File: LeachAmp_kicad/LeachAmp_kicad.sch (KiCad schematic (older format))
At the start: 119 parts, among them J1 Conn_01x12_Female, J2 Conn_01x04_Female, J3 Conn_01x03_Female, J4 Conn_01x03_Female, Q1 BC546, Q10 MPSA06, Q11 MPSA56, Q12 BF470, Q13 BF469, Q14 BF469, Q15 BF470, Q16 MJE15030, Q17 MJE15031, Q2 BC546, Q3 BC556, Q4 BC556, Q5 BC546, Q6 BC556, Q7 BD139, Q8 BC556, Q9 BC546, T1 MJL3281, T2 MJL3201, T3 MJL3281, T4 MJL3201

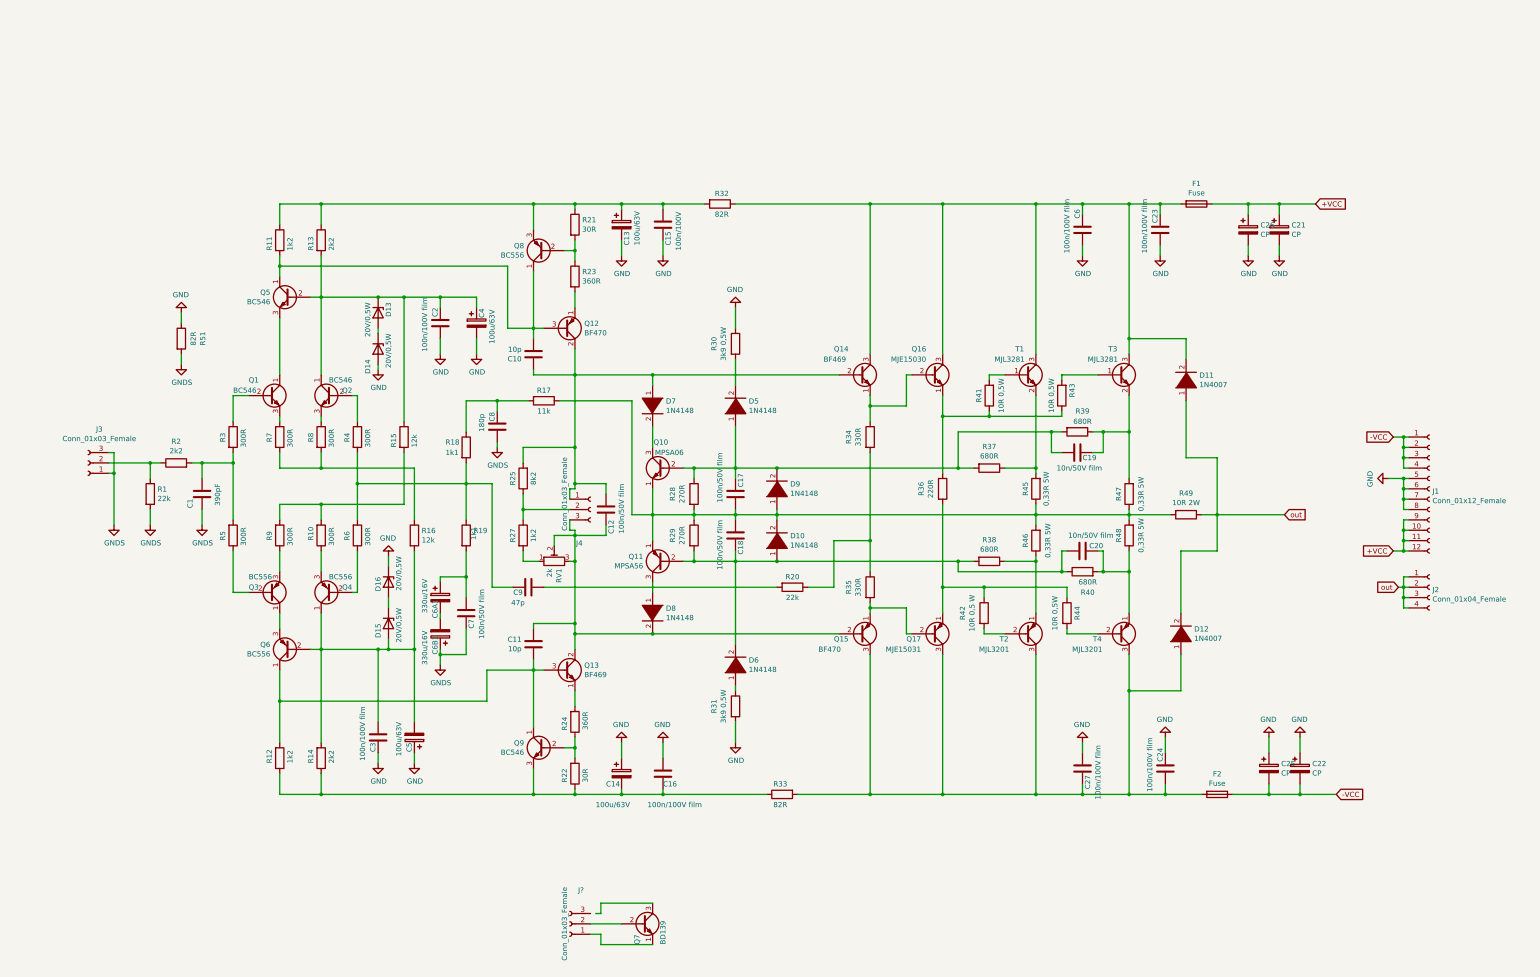
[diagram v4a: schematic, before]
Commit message: Kondenzatory v prostred
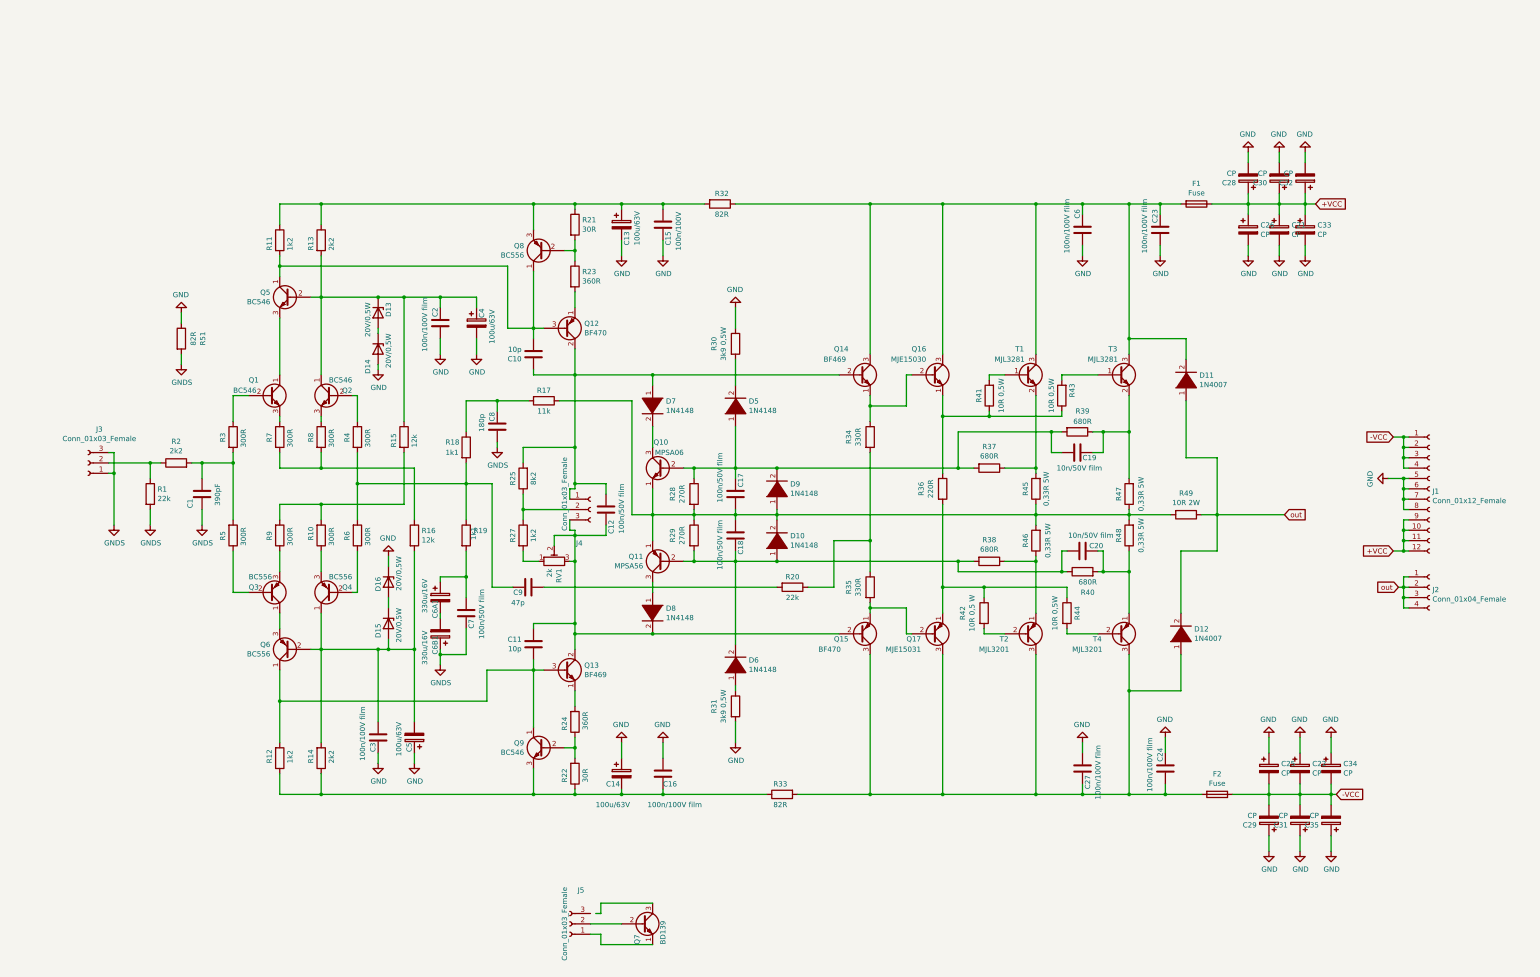
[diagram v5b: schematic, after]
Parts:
- added C28, C29, C30, C31, C32, C33, C34, C35: CP, Capacitor_THT:CP_Radial_D25.0mm_P10.00mm_SnapIn, symbol Device:CP
- C21, C22, C25, C26: footprint Capacitor_THT:CP_Radial_D35.0mm_P10.00mm_SnapIn -> Capacitor_THT:CP_Radial_D25.0mm_P10.00mm_SnapIn
- gave numbers to parts that had none: 1
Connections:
- net +VCC: now also C28.1, C30.1, C32.1, C33.1
- net -VCC: now also C29.2, C31.2, C34.2, C35.2
- net GND: now also C28.2, C29.1, C30.2, C31.1, C32.2, C33.2, C34.1, C35.1
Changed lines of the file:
@@
 F 0 "C21" H 13318 2596 50  0000 L CNN
 F 1 "CP" H 13318 2505 50  0000 L CNN
-F 2 "Capacitor_THT:CP_Radial_D35.0mm_P10.00mm_SnapIn" H 13238 2400 50  0001 C CNN
+F 2 "Capacitor_THT:CP_Radial_D25.0mm_P10.00mm_SnapIn" H 13238 2400 50  0001 C CNN
 F 3 "~" H 13200 2550 50  0001 C CNN
 	1    13200 2550
@@
 F 0 "C22" H 13518 7796 50  0000 L CNN
 F 1 "CP" H 13518 7705 50  0000 L CNN
-F 2 "Capacitor_THT:CP_Radial_D35.0mm_P10.00mm_SnapIn" H 13438 7600 50  0001 C CNN
+F 2 "Capacitor_THT:CP_Radial_D25.0mm_P10.00mm_SnapIn" H 13438 7600 50  0001 C CNN
 F 3 "~" H 13400 7750 50  0001 C CNN
 	1    13400 7750
@@
 F 0 "C25" H 13218 7796 50  0000 L CNN
 F 1 "CP" H 13218 7705 50  0000 L CNN
-F 2 "Capacitor_THT:CP_Radial_D35.0mm_P10.00mm_SnapIn" H 13138 7600 50  0001 C CNN
+F 2 "Capacitor_THT:CP_Radial_D25.0mm_P10.00mm_SnapIn" H 13138 7600 50  0001 C CNN
 F 3 "~" H 13100 7750 50  0001 C CNN
 	1    13100 7750
@@
 F 0 "C26" H 13018 2596 50  0000 L CNN
 F 1 "CP" H 13018 2505 50  0000 L CNN
-F 2 "Capacitor_THT:CP_Radial_D35.0mm_P10.00mm_SnapIn" H 12938 2400 50  0001 C CNN
+F 2 "Capacitor_THT:CP_Radial_D25.0mm_P10.00mm_SnapIn" H 12938 2400 50  0001 C CNN
 F 3 "~" H 12900 2550 50  0001 C CNN
 	1    12900 2550
@@
 	12250 2300 12050 2300
 Wire Wire Line
-	13550 2300 13200 2300
+	13550 2300 13450 2300
 Connection ~ 13200 2300
 $Comp
@@
 	12450 8000 12100 8000
 Wire Wire Line
-	13750 8000 13400 8000
+	13750 8000 13700 8000
 Connection ~ 13400 8000
 Text GLabel 13250 5300 2    50   Input ~ 0
@@
 	6350 5050 6400 5050
 $Comp
-L Connector:Conn_01x03_Female J?
+L Connector:Conn_01x03_Female J5
 U 1 1 6004D92D
 P 6350 9250
-F 0 "J?" H 6242 8925 50  0000 C CNN
+F 0 "J5" H 6242 8925 50  0000 C CNN
 F 1 "Conn_01x03_Female" V 6400 9250 50  0000 C CNN
 F 2 "Connector_Molex:Molex_KK-254_AE-6410-03A_1x03_P2.54mm_Vertical" H 6350 9250 50  0001 C CNN
@@
 Wire Wire Line
 	6850 9250 6550 9250
+$Comp
+L Device:CP C28
+U 1 1 600E297A
+P 12900 2050
+F 0 "C28" H 13018 2096 50  0000 L CNN
+F 1 "CP" H 13018 2005 50  0000 L CNN
+F 2 "Capacitor_THT:CP_Radial_D25.0mm_P10.00mm_SnapIn" H 12938 1900 50  0001 C CNN
+F 3 "~" H 12900 2050 50  0001 C CNN
+	1    12900 2050
+	-1   0    0    1
+$EndComp
+$Comp
+L Device:CP C30
+U 1 1 600E3916
+P 13200 2050
+F 0 "C30" H 13318 2096 50  0000 L CNN
+F 1 "CP" H 13318 2005 50  0000 L CNN
+F 2 "Capacitor_THT:CP_Radial_D25.0mm_P10.00mm_SnapIn" H 13238 1900 50  0001 C CNN
+F 3 "~" H 13200 2050 50  0001 C CNN
+	1    13200 2050
+	-1   0    0    1
+$EndComp
+$Comp
+L Device:CP C32
+U 1 1 600E3C0C
+P 13450 2050
+F 0 "C32" H 13568 2096 50  0000 L CNN
+F 1 "CP" H 13568 2005 50  0000 L CNN
+F 2 "Capacitor_THT:CP_Radial_D25.0mm_P10.00mm_SnapIn" H 13488 1900 50  0001 C CNN
+F 3 "~" H 13450 2050 50  0001 C CNN
+	1    13450 2050
+	-1   0    0    1
+$EndComp
+$Comp
+L Device:CP C33
+U 1 1 600E4223
+P 13450 2550
+F 0 "C33" H 13568 2596 50  0000 L CNN
+F 1 "CP" H 13568 2505 50  0000 L CNN
+F 2 "Capacitor_THT:CP_Radial_D25.0mm_P10.00mm_SnapIn" H 13488 2400 50  0001 C CNN
+F 3 "~" H 13450 2550 50  0001 C CNN
+	1    13450 2550
+	1    0    0    -1
+$EndComp
+$Comp
+L power:GND #PWR0102
+U 1 1 600E4591
+P 13450 2800
+F 0 "#PWR0102" H 13450 2550 50  0001 C CNN
+F 1 "GND" H 13455 2627 50  0000 C CNN
+F 2 "" H 13450 2800 50  0001 C CNN
+F 3 "" H 13450 2800 50  0001 C CNN
+	1    13450 2800
+	1    0    0    -1
+$EndComp
+$Comp
+L power:GND #PWR0106
+U 1 1 600E487A
+P 13450 1800
+F 0 "#PWR0106" H 13450 1550 50  0001 C CNN
+F 1 "GND" H 13455 1627 50  0000 C CNN
+F 2 "" H 13450 1800 50  0001 C CNN
+F 3 "" H 13450 1800 50  0001 C CNN
+	1    13450 1800
+	-1   0    0    1
+$EndComp
+$Comp
+L power:GND #PWR0107
+U 1 1 600E4FE6
+P 13200 1800
+F 0 "#PWR0107" H 13200 1550 50  0001 C CNN
+F 1 "GND" H 13205 1627 50  0000 C CNN
+F 2 "" H 13200 1800 50  0001 C CNN
+F 3 "" H 13200 1800 50  0001 C CNN
+	1    13200 1800
+	-1   0    0    1
+$EndComp
+$Comp
+L power:GND #PWR0108
+U 1 1 600E532F
+P 12900 1800
+F 0 "#PWR0108" H 12900 1550 50  0001 C CNN
+F 1 "GND" H 12905 1627 50  0000 C CNN
+F 2 "" H 12900 1800 50  0001 C CNN
+F 3 "" H 12900 1800 50  0001 C CNN
+	1    12900 1800
+	-1   0    0    1
+$EndComp
+Wire Wire Line
+	13450 1900 13450 1800
+Wire Wire Line
+	13200 1900 13200 1800
+Wire Wire Line
+	12900 1900 12900 1800
+Wire Wire Line
+	13200 2200 13200 2300
+Wire Wire Line
+	12900 2200 12900 2300
+Wire Wire Line
+	13450 2200 13450 2300
+Connection ~ 13450 2300
+Wire Wire Line
+	13450 2300 13200 2300
+Wire Wire Line
+	13450 2400 13450 2300
+$Comp
+L power:GND #PWR0109
+U 1 1 601F53FE
+P 13700 7450
+F 0 "#PWR0109" H 13700 7200 50  0001 C CNN
+F 1 "GND" H 13705 7277 50  0000 C CNN
+F 2 "" H 13700 7450 50  0001 C CNN
+F 3 "" H 13700 7450 50  0001 C CNN
+	1    13700 7450
+	-1   0    0    1
+$EndComp
+$Comp
+L Device:CP C34
+U 1 1 601F5404
+P 13700 7750
+F 0 "C34" H 13818 7796 50  0000 L CNN
+F 1 "CP" H 13818 7705 50  0000 L CNN
+F 2 "Capacitor_THT:CP_Radial_D25.0mm_P10.00mm_SnapIn" H 13738 7600 50  0001 C CNN
+F 3 "~" H 13700 7750 50  0001 C CNN
+	1    13700 7750
+	1    0    0    -1
+$EndComp
+Wire Wire Line
+	13700 7600 13700 7450
+$Comp
+L power:GND #PWR0110
+U 1 1 60218240
+P 13100 8550
+F 0 "#PWR0110" H 13100 8300 50  0001 C CNN
+F 1 "GND" H 13105 8377 50  0000 C CNN
+F 2 "" H 13100 8550 50  0001 C CNN
+F 3 "" H 13100 8550 50  0001 C CNN
+	1    13100 8550
+	1    0    0    -1
+$EndComp
+$Comp
+L Device:CP C29
+U 1 1 60218246
+P 13100 8250
+F 0 "C29" H 13218 8296 50  0000 L CNN
+F 1 "CP" H 13218 8205 50  0000 L CNN
+F 2 "Capacitor_THT:CP_Radial_D25.0mm_P10.00mm_SnapIn" H 13138 8100 50  0001 C CNN
+F 3 "~" H 13100 8250 50  0001 C CNN
+	1    13100 8250
+	-1   0    0    1
+$EndComp
+Wire Wire Line
+	13100 8400 13100 8550
+$Comp
+L power:GND #PWR0111
+U 1 1 6023A713
+P 13400 8550
+F 0 "#PWR0111" H 13400 8300 50  0001 C CNN
+F 1 "GND" H 13405 8377 50  0000 C CNN
+F 2 "" H 13400 8550 50  0001 C CNN
+F 3 "" H 13400 8550 50  0001 C CNN
+	1    13400 8550
+	1    0    0    -1
+$EndComp
+$Comp
+L Device:CP C31
+U 1 1 6023A719
+P 13400 8250
+F 0 "C31" H 13518 8296 50  0000 L CNN
+F 1 "CP" H 13518 8205 50  0000 L CNN
+F 2 "Capacitor_THT:CP_Radial_D25.0mm_P10.00mm_SnapIn" H 13438 8100 50  0001 C CNN
+F 3 "~" H 13400 8250 50  0001 C CNN
+	1    13400 8250
+	-1   0    0    1
+$EndComp
+Wire Wire Line
+	13400 8400 13400 8550
+$Comp
+L power:GND #PWR0112
+U 1 1 6025D321
+P 13700 8550
+F 0 "#PWR0112" H 13700 8300 50  0001 C CNN
+F 1 "GND" H 13705 8377 50  0000 C CNN
+F 2 "" H 13700 8550 50  0001 C CNN
+F 3 "" H 13700 8550 50  0001 C CNN
+	1    13700 8550
+	1    0    0    -1
+$EndComp
+$Comp
+L Device:CP C35
+U 1 1 6025D327
+P 13700 8250
+F 0 "C35" H 13818 8296 50  0000 L CNN
+F 1 "CP" H 13818 8205 50  0000 L CNN
+F 2 "Capacitor_THT:CP_Radial_D25.0mm_P10.00mm_SnapIn" H 13738 8100 50  0001 C CNN
+F 3 "~" H 13700 8250 50  0001 C CNN
+	1    13700 8250
+	-1   0    0    1
+$EndComp
+Wire Wire Line
+	13700 8400 13700 8550
+Wire Wire Line
+	13700 7900 13700 8000
+Connection ~ 13700 8000
+Wire Wire Line
+	13700 8000 13400 8000
+Wire Wire Line
+	13700 8100 13700 8000
+Wire Wire Line
+	13400 8100 13400 8000
+Wire Wire Line
+	13100 8100 13100 8000
+Wire Wire Line
+	13450 2800 13450 2700
 $EndSCHEMATC
